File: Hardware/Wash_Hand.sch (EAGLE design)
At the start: 71 parts, among them IC1 LM358D, IC2 LP298XS, IC3 405016TSSOP, J1 I2C, J2 ICSP, J3 SPI, J4 9V_CONN, J5 EXT_VCC, J6 6_PIN_SERIAL_CABLEPTH, Q1 16.0 Mhz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

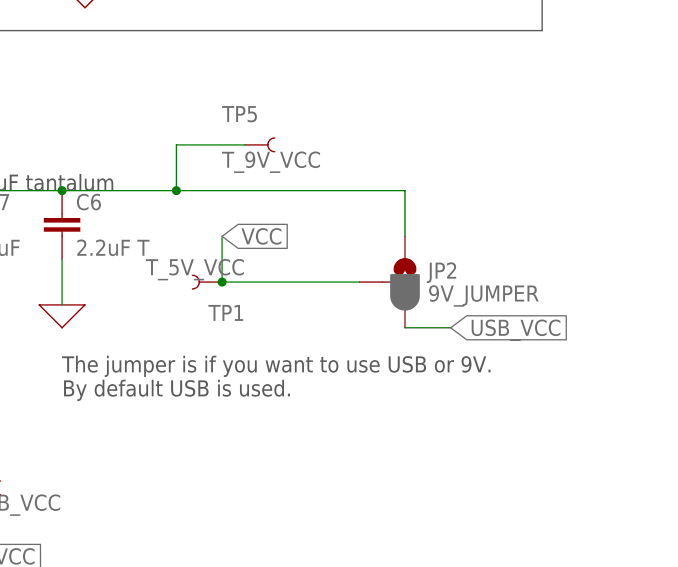
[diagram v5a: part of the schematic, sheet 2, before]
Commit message: Board/Schematic: Replace 9V/5V SMT pad with normally closed
Makes it easier to debug as the solder will close both
of. But if we are doing production runs we would enable/disable
the connectors by not populating the components (like the
whole 9V power-plant).

Signed-off-by: Konrad Rzeszutek Wilk <konrad@kernel.org>
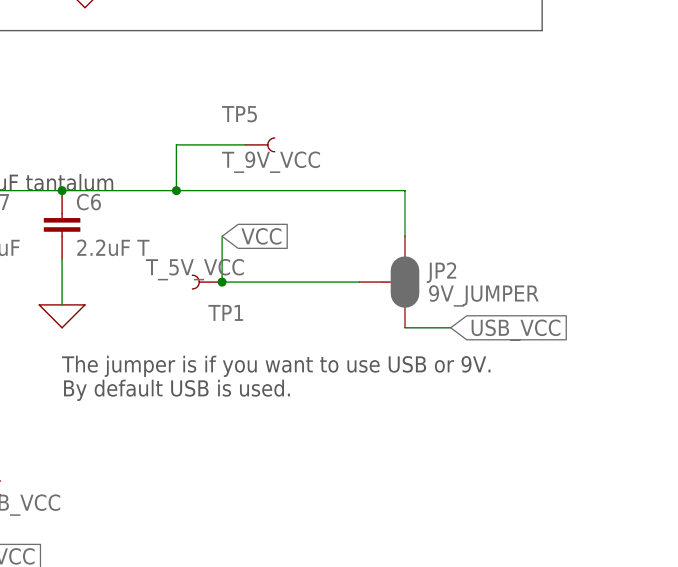
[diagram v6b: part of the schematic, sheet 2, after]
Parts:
- JP2: device SparkFun-Jumpers:JUMPER-SMT_3_1-NC_PASTE_SILK -> SparkFun-Jumpers:JUMPER-SMT_3_2-NC_PASTE_SILK
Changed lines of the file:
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@@
 <part name="J4" library="SparkFun-Connectors" library_urn="urn:adsk.eagle:library:513" deviceset="CONN_02" device="" package3d_urn="urn:adsk.eagle:package:38039/1" value="9V_CONN"/>
 <part name="X_13" library="ngspice-simulation" library_urn="urn:adsk.eagle:library:527439" deviceset="GND" device=""/>
-<part name="JP2" library="SparkFun-Jumpers" library_urn="urn:adsk.eagle:library:528" deviceset="JUMPER-SMT_3_1-NC_PASTE" device="_SILK" package3d_urn="urn:adsk.eagle:package:39293/1" value="9V_JUMPER"/>
+<part name="JP2" library="SparkFun-Jumpers" library_urn="urn:adsk.eagle:library:528" deviceset="JUMPER-SMT_3_2-NC_PASTE" device="_SILK" package3d_urn="urn:adsk.eagle:package:39294/1" value="9V_JUMPER"/>
 <part name="JP3" library="SparkFun-Jumpers" library_urn="urn:adsk.eagle:library:528" deviceset="JUMPER-SMT_2_NC_PASTE" device="_SILK" package3d_urn="urn:adsk.eagle:package:39282/1" value="ENA_INT_D0"/>
 <part name="JP4" library="SparkFun-Jumpers" library_urn="urn:adsk.eagle:library:528" deviceset="JUMPER-SMT_2_NC_PASTE" device="_SILK" package3d_urn="urn:adsk.eagle:package:39282/1" value="ENA_INT_SENSOR"/>

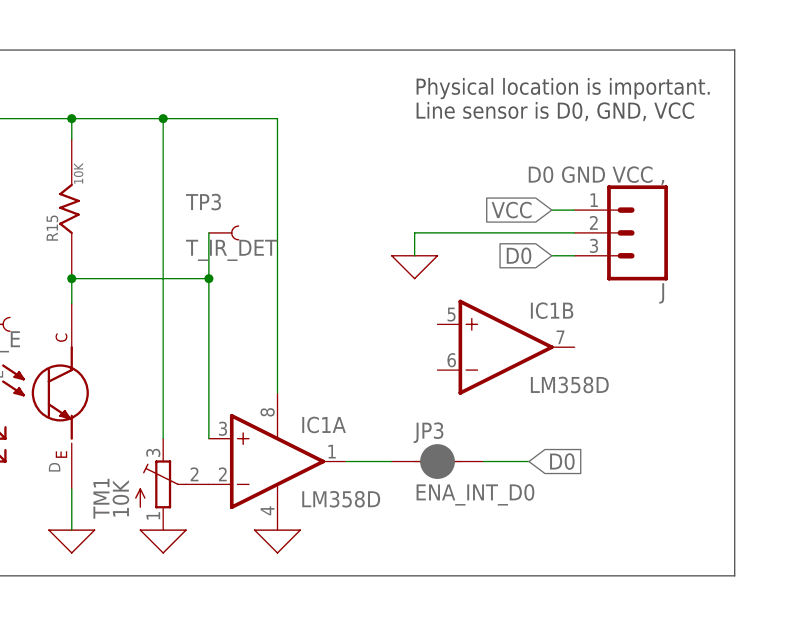
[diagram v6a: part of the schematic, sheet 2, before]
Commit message: Board/Schematic: Add a LED on the line-sensor
..when we have detected a change.

Signed-off-by: Konrad Rzeszutek Wilk <konrad@kernel.org>
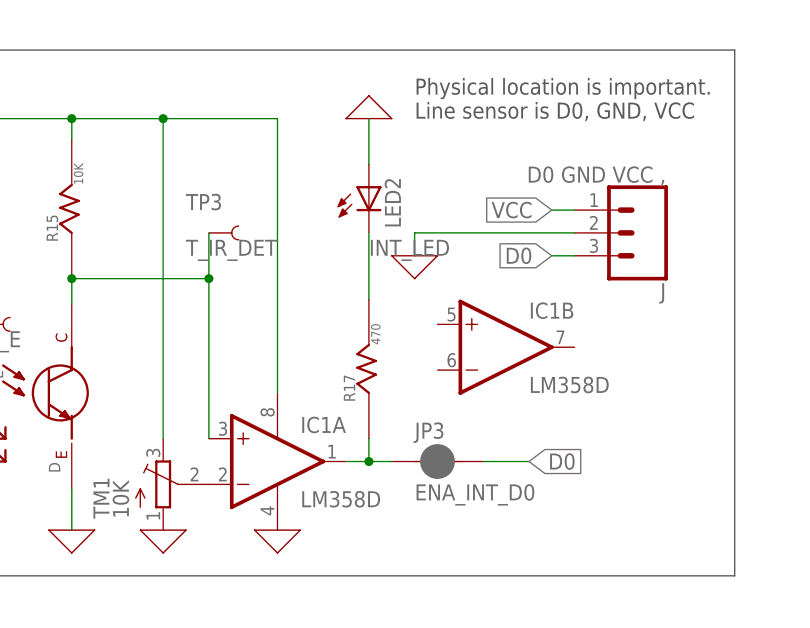
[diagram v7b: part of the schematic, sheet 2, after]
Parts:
- added LED2: (no value), adafruit:LEDSMT1206
- added R17: 470, darnok_common:RESISTORR1206
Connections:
- new net INT_LED: LED2.C, R17.R_2
- net 0: now also LED2.A
- net D0: now also R17.R_1
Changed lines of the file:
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@@
 <part name="LED1" library="adafruit" library_urn="urn:adsk.eagle:library:420" deviceset="LED" device="SMT1206" package3d_urn="urn:adsk.eagle:package:6240349/1" value="RED"/>
 <part name="R16" library="darnok_common" deviceset="RESISTOR" device="R1206" value="1K"/>
+<part name="R17" library="darnok_common" deviceset="RESISTOR" device="R1206" value="470"/>
+<part name="LED2" library="adafruit" library_urn="urn:adsk.eagle:library:420" deviceset="LED" device="SMT1206" package3d_urn="urn:adsk.eagle:package:6240349/1"/>
+<part name="X_31" library="ngspice-simulation" library_urn="urn:adsk.eagle:library:527439" deviceset="GND" device=""/>
 </parts>
 <sheets>
@@
 <attribute name="VALUE" x="218.44" y="139.7" size="1.778" layer="96"/>
 </instance>
+<instance part="R17" gate="G$1" x="200.66" y="139.7" smashed="yes" rot="R90">
+<attribute name="NAME" x="199.136" y="138.684" size="1.27" layer="95" rot="R90"/>
+<attribute name="VALUE" x="201.93" y="145.034" size="1.016" layer="96" rot="R90"/>
+</instance>
+<instance part="LED2" gate="G$1" x="200.66" y="162.56" smashed="yes">
+<attribute name="NAME" x="204.216" y="157.988" size="1.778" layer="95" rot="R90"/>
+<attribute name="VALUE" x="206.375" y="157.988" size="1.778" layer="96" rot="R90"/>
+</instance>
+<instance part="X_31" gate="G$1" x="200.66" y="170.18" smashed="yes" rot="R180"/>
 </instances>
 <busses>
@@
 <pinref part="X_1" gate="G$1" pin="0"/>
 </segment>
+<segment>
+<pinref part="X_31" gate="G$1" pin="0"/>
+<pinref part="LED2" gate="G$1" pin="A"/>
+<wire x1="200.66" y1="170.18" x2="200.66" y2="165.1" width="0.1524" layer="91"/>
+</segment>
 </net>
 <net name="D0" class="0">
@@
 <pinref part="JP3" gate="G$1" pin="1"/>
 <pinref part="IC1" gate="A" pin="OUT"/>
-<wire x1="198.12" y1="132.08" x2="203.2" y2="132.08" width="0.1524" layer="91"/>
+<wire x1="198.12" y1="132.08" x2="200.66" y2="132.08" width="0.1524" layer="91"/>
+<pinref part="R17" gate="G$1" pin="R_1"/>
+<wire x1="200.66" y1="132.08" x2="203.2" y2="132.08" width="0.1524" layer="91"/>
+<wire x1="200.66" y1="132.08" x2="200.66" y2="134.62" width="0.1524" layer="91"/>
+<junction x="200.66" y="132.08"/>
 </segment>
 <segment>
@@
 </segment>
 </net>
+<net name="INT_LED" class="0">
+<segment>
+<pinref part="LED2" gate="G$1" pin="C"/>
+<pinref part="R17" gate="G$1" pin="R_2"/>
+<wire x1="200.66" y1="157.48" x2="200.66" y2="150.114" width="0.1524" layer="91"/>
+<label x="200.66" y="154.94" size="1.778" layer="95"/>
+</segment>
+</net>

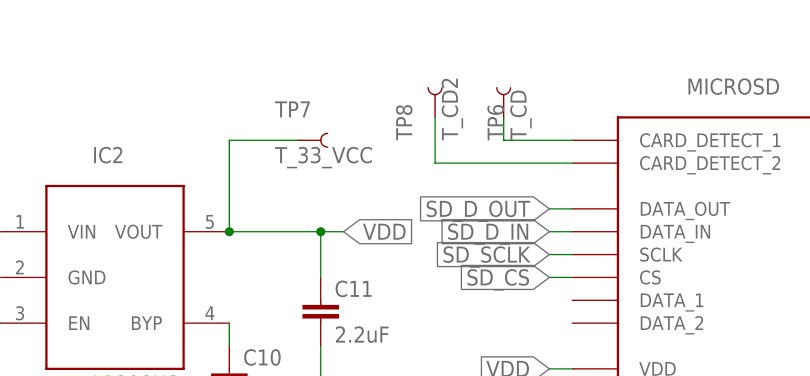
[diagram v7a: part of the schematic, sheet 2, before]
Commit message: Board/Schematic: Make CD_1 and CD_2 connect to ADC6
And do a pull-up resistor on CD_2.

Signed-off-by: Konrad Rzeszutek Wilk <konrad@kernel.org>
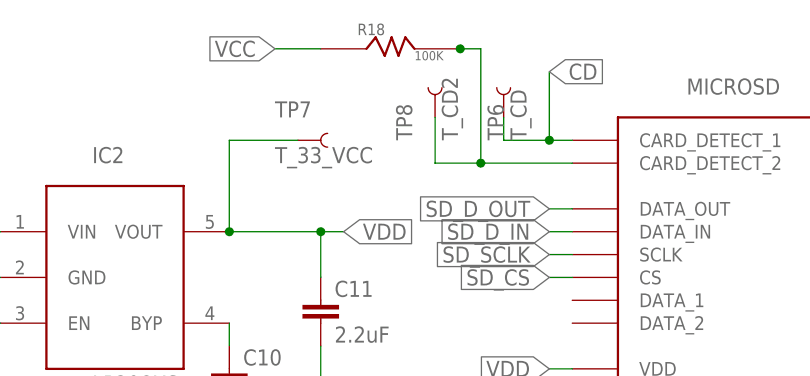
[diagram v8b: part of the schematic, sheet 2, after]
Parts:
- added R18: 100K, darnok_common:RESISTORR1206
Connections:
- removed net N$1: MICROSD.CARD_DETECT_1, TP6.1
- new net CD: MICROSD.CARD_DETECT_1, TP6.1, U2.ADC6
- net N$2: now also R18.R_2
- net VCC: now also R18.R_1
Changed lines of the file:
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@@
 <part name="LED2" library="adafruit" library_urn="urn:adsk.eagle:library:420" deviceset="LED" device="SMT1206" package3d_urn="urn:adsk.eagle:package:6240349/1"/>
 <part name="X_31" library="ngspice-simulation" library_urn="urn:adsk.eagle:library:527439" deviceset="GND" device=""/>
+<part name="R18" library="darnok_common" deviceset="RESISTOR" device="R1206" value="100K"/>
 </parts>
 <sheets>
@@
 <pinref part="LED1" gate="G$1" pin="C"/>
 <wire x1="66.04" y1="127" x2="66.04" y2="124.46" width="0.1524" layer="91"/>
+</segment>
+</net>
+<net name="CD" class="0">
+<segment>
+<pinref part="U2" gate="U$1" pin="ADC6"/>
+<wire x1="185.42" y1="142.24" x2="187.96" y2="142.24" width="0.1524" layer="91"/>
+<label x="187.96" y="142.24" size="1.778" layer="95" xref="yes"/>
 </segment>
 </net>
@@
 </instance>
 <instance part="X_31" gate="G$1" x="200.66" y="170.18" smashed="yes" rot="R180"/>
+<instance part="R18" gate="G$1" x="58.42" y="182.88" smashed="yes">
+<attribute name="NAME" x="57.404" y="184.404" size="1.27" layer="95"/>
+<attribute name="VALUE" x="63.754" y="181.61" size="1.016" layer="96"/>
+</instance>
 </instances>
 <busses>
@@
 <wire x1="223.52" y1="160.02" x2="220.98" y2="160.02" width="0.1524" layer="91"/>
 <label x="220.98" y="160.02" size="1.778" layer="95" rot="R180" xref="yes"/>
+</segment>
+<segment>
+<pinref part="R18" gate="G$1" pin="R_1"/>
+<wire x1="53.34" y1="182.88" x2="48.26" y2="182.88" width="0.1524" layer="91"/>
+<label x="48.26" y="182.88" size="1.778" layer="95" rot="R180" xref="yes"/>
 </segment>
 </net>
@@
 </segment>
 </net>
-<net name="N$1" class="0">
+<net name="CD" class="0">
 <segment>
 <pinref part="TP6" gate="G$1" pin="1"/>
 <wire x1="73.66" y1="172.72" x2="73.66" y2="175.26" width="0.1524" layer="91"/>
 <pinref part="MICROSD" gate="A" pin="CARD_DETECT_1"/>
-<wire x1="81.28" y1="172.72" x2="73.66" y2="172.72" width="0.1524" layer="91"/>
-</segment>
-</net>
-<net name="N$2" class="0">
-<segment>
-<pinref part="TP8" gate="G$1" pin="1"/>
-<wire x1="66.04" y1="170.18" x2="66.04" y2="175.26" width="0.1524" layer="91"/>
-<pinref part="MICROSD" gate="A" pin="CARD_DETECT_2"/>
-<wire x1="81.28" y1="170.18" x2="66.04" y2="170.18" width="0.1524" layer="91"/>
+<label x="78.74" y="180.34" size="1.778" layer="95" xref="yes"/>
+<wire x1="81.28" y1="172.72" x2="78.74" y2="172.72" width="0.1524" layer="91"/>
+<wire x1="78.74" y1="172.72" x2="73.66" y2="172.72" width="0.1524" layer="91"/>
+<wire x1="78.74" y1="180.34" x2="78.74" y2="172.72" width="0.1524" layer="91"/>
+<junction x="78.74" y="172.72"/>
 </segment>
 </net>
@@
 </segment>
 </net>
+<net name="N$2" class="0">
+<segment>
+<pinref part="TP8" gate="G$1" pin="1"/>
+<wire x1="66.04" y1="175.26" x2="66.04" y2="170.18" width="0.1524" layer="91"/>
+<pinref part="MICROSD" gate="A" pin="CARD_DETECT_2"/>
+<wire x1="66.04" y1="170.18" x2="71.12" y2="170.18" width="0.1524" layer="91"/>
+<wire x1="71.12" y1="170.18" x2="81.28" y2="170.18" width="0.1524" layer="91"/>
+<wire x1="71.12" y1="170.18" x2="71.12" y2="182.88" width="0.1524" layer="91"/>
+<junction x="71.12" y="170.18"/>
+<pinref part="R18" gate="G$1" pin="R_2"/>
+<wire x1="68.58" y1="182.88" x2="68.834" y2="182.88" width="0.1524" layer="91"/>
+<wire x1="71.12" y1="182.88" x2="68.834" y2="182.88" width="0.1524" layer="91"/>
+<junction x="68.834" y="182.88"/>
+</segment>
+</net>
